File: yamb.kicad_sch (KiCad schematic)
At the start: 5 parts, among them J1 Barrel_Jack, P1 USB_C_Plug_USB2.0

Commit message: still lots of errors
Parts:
- added U1: TPS3808DBV, Package_TO_SOT_SMD:SOT-23-6, symbol Power_Supervisor:TPS3808DBV
- RAK1: value ~ -> U4
- U2: renamed from Voltaic MPPT; value ~ -> MPPT
- U3: renamed from Voltaic SVR; value ~ -> VSVR
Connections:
- net +BATT is gone; now on net BATT: U3.5 (VBAT)
- net -BATT is gone; now on net GND: U3.4 (GND)
- net +5V: now also P1.A4 (VBUS), P1.A9 (VBUS), P1.B4 (VBUS), P1.B9 (VBUS); no longer RAK1.43 (VDD_NRF), RAK1.44 (VBAT_NRF), U2.11 (VLOAD), U3.12 (VLOAD)
- net 7-20V: no longer J1.2, P1.A1 (GND), P1.A12 (GND), P1.B1 (GND), P1.B12 (GND), RAK1.14 (GND), RAK1.22 (GND), RAK1.35 (GND), RAK1.36 (GND), RAK1.42 (GND), U2.10 (GND), U2.12 (GND), U2.14 (GND), U2.16 (GND), U2.17 (GND), U3.13 (GND), U3.14 (GND), U3.16 (GND), U3.17 (GND), U3.7 (GND), U3.8 (GND)
- net SDA: now also RAK1.4 (I2C_SDA); no longer RAK1.6 (UART2_RX)
- net GND: now reaches P1.S1 (SHIELD)
- net GND: now also J1.2, P1.A1 (GND), P1.A12 (GND), P1.B1 (GND), P1.B12 (GND), RAK1.14 (GND), RAK1.16 (GND), RAK1.22 (GND), RAK1.35 (GND), RAK1.36 (GND), RAK1.38 (GND), RAK1.42 (GND), U2.10 (GND), U2.12 (GND), U2.14 (GND), U2.16 (GND), U2.17 (GND), U2.4 (GND), U2.6 (GND), U2.8 (GND), U3.13 (GND), U3.14 (GND), U3.16 (GND), U3.17 (GND), U3.7 (GND), U3.8 (GND), U1.2 (GND)
- net RESET: now reaches RAK1.17 (NRF_RESET)
- net RESET: now also U1.1 (~{RESET})
- net +3.3V: now reaches RAK1.20 (VBAT_SX)
- net +3.3V: now also RAK1.21 (VBAT_IO_SX), RAK1.43 (VDD_NRF), U2.11 (VLOAD), U2.9 (VLOAD), U3.12 (VLOAD), U1.5 (SENSE)
- net BATT: now reaches U2.5 (VBAT)
- net BATT: now also RAK1.44 (VBAT_NRF), U2.7 (VBAT)
- net 3V3 renamed 3V3_I2C
- new net VBUS: U1.6 (VDD)
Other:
- moved on the sheet: U2

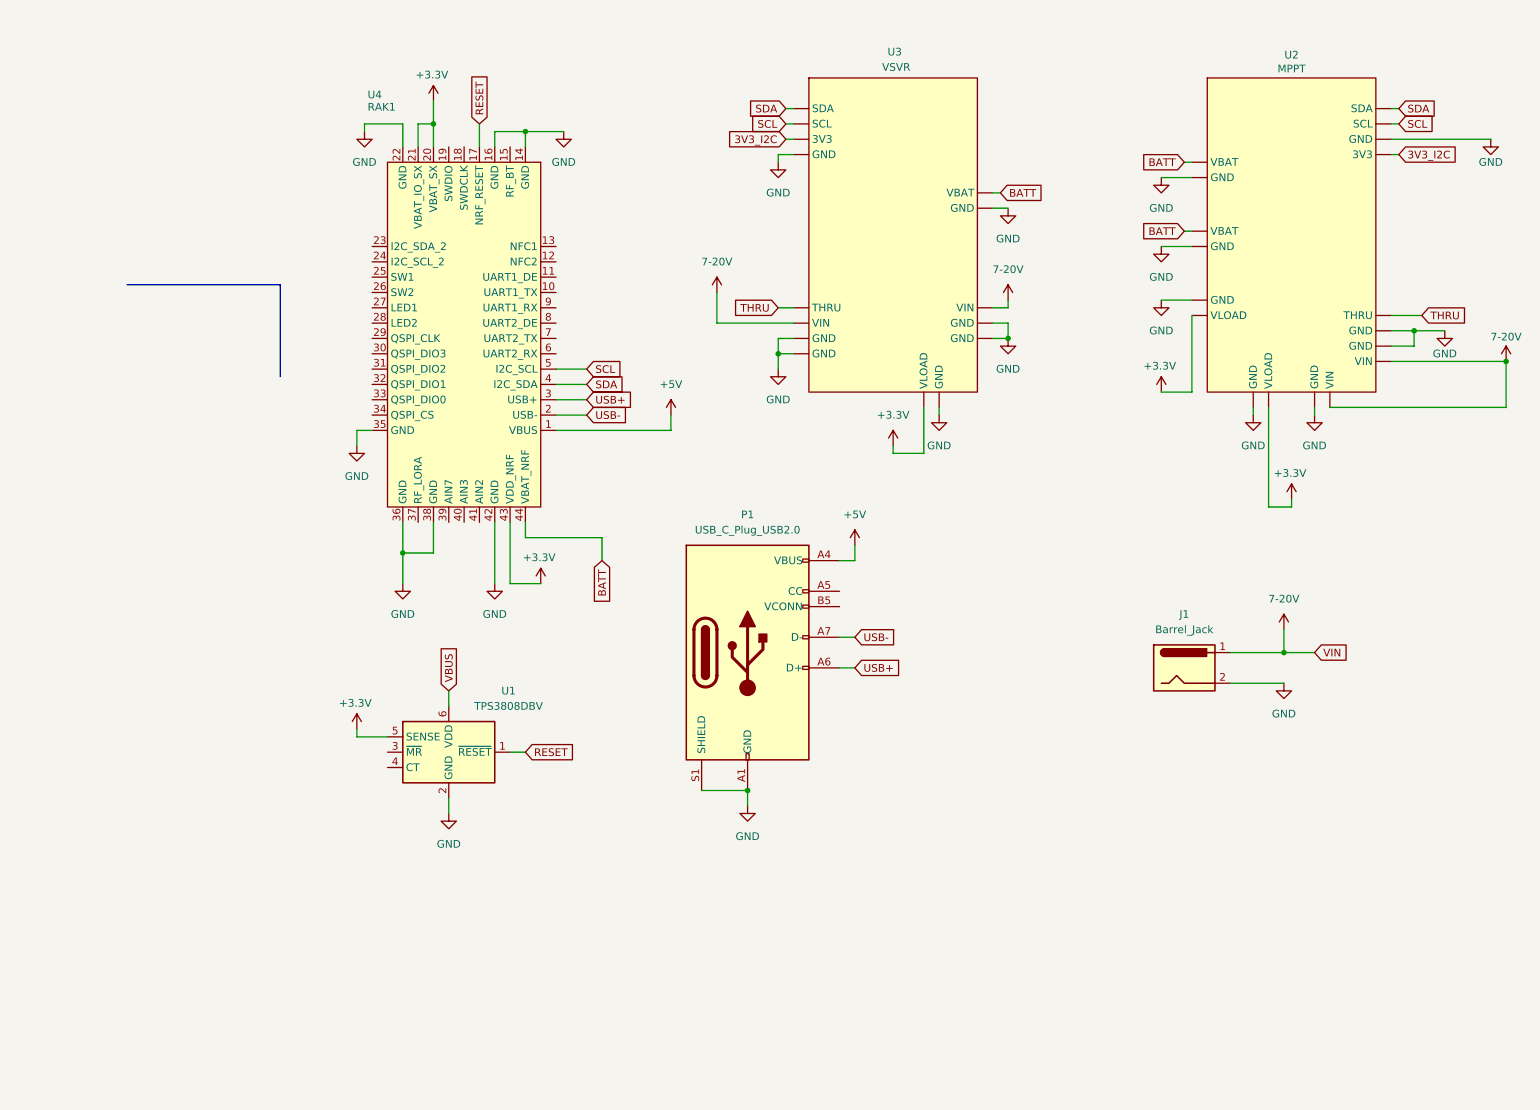
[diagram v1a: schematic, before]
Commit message: voltaic footprints, adding to schematic
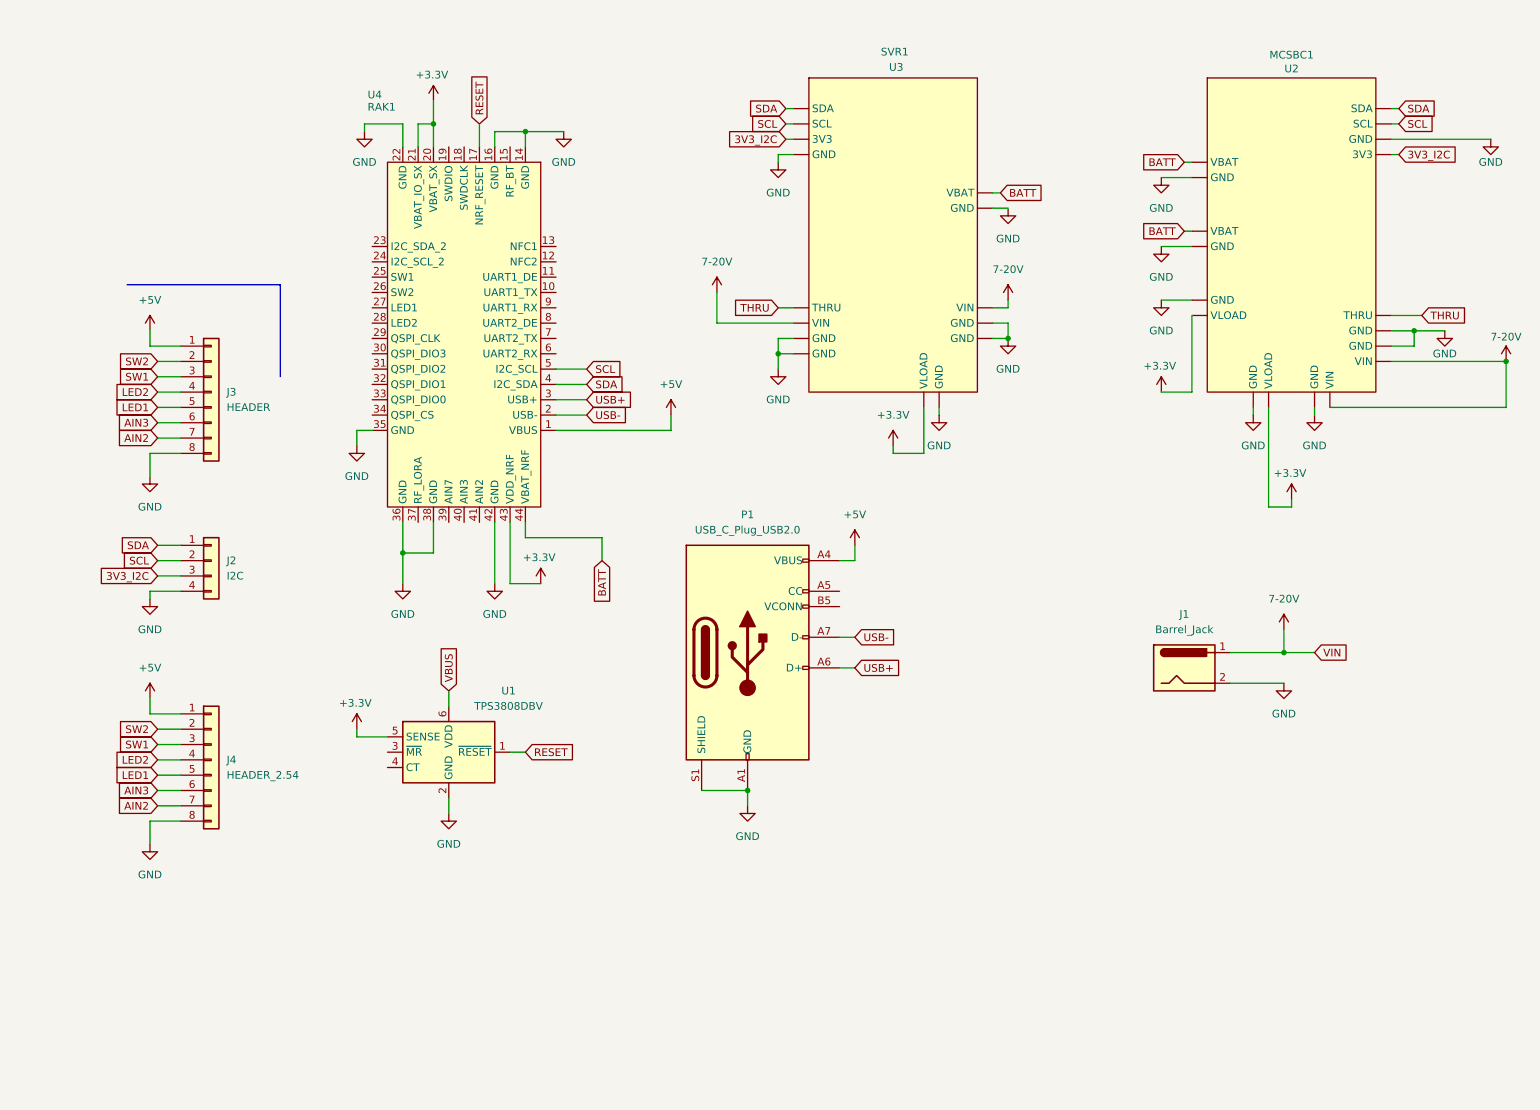
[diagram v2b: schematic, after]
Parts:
- added J2: I2C, Connector_JST:JST_PH_B4B-PH-K_1x04_P2.00mm_Vertical, symbol Connector_Generic:Conn_01x04
- added J3: HEADER, Connector_JST:JST_PH_B8B-PH-K_1x08_P2.00mm_Vertical, symbol Connector_Generic:Conn_01x08
- added J4: HEADER_2.54, Connector_PinHeader_2.54mm:PinHeader_1x08_P2.54mm_Vertical, symbol Connector_Generic:Conn_01x08
- J1: footprint (none) -> Connector_BarrelJack:SWITCHCRAFT_PC722A
- MCSBC1: renamed from U2; value MPPT -> U2; footprint (none) -> Converter_DCDC:Voltaic_MCSBC; now in the parts list
- P1: footprint (none) -> Connector_USB:USB_C_Receptacle_G-Switch_GT-USB-7051x
- RAK1: footprint (none) -> RF_Module:RAK4630
- SVR1: renamed from U3; value VSVR -> U3; footprint (none) -> Converter_DCDC:Voltaic_SVR; now in the parts list
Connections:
- net +5V: now also J3.1 (Pin_1), J4.1 (Pin_1)
- net 3V3_I2C: now also J2.3 (Pin_3)
- net GND: now also J2.4 (Pin_4), J3.8 (Pin_8), J4.8 (Pin_8)
- net SCL: now also J2.2 (Pin_2)
- net SDA: now also J2.1 (Pin_1)
- new net AIN2: J3.7 (Pin_7), J4.7 (Pin_7)
- new net AIN3: J3.6 (Pin_6), J4.6 (Pin_6)
- new net LED1: J3.5 (Pin_5), J4.5 (Pin_5)
- new net LED2: J3.4 (Pin_4), J4.4 (Pin_4)
- new net SW1: J3.3 (Pin_3), J4.3 (Pin_3)
- new net SW2: J3.2 (Pin_2), J4.2 (Pin_2)

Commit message: additional footprints for reset, power switch, correct USB-C symbol for footprint, bypass jumpers for watchdog and pwr switch
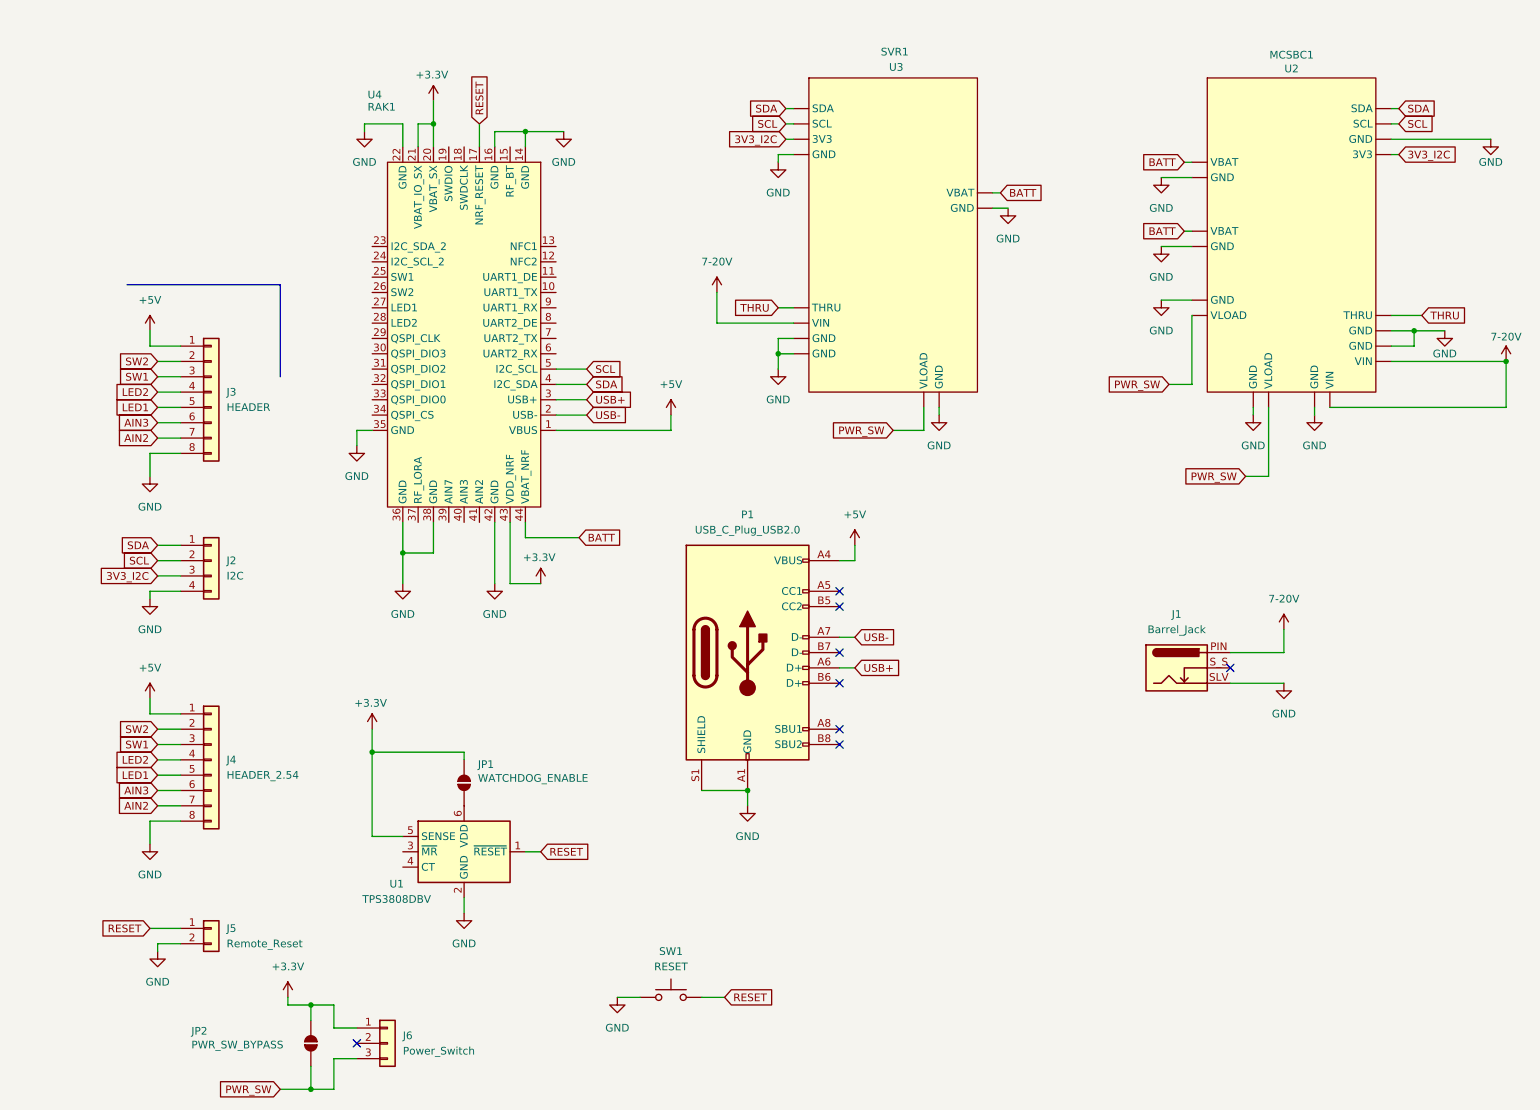
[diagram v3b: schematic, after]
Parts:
- added J5: Remote_Reset, Connector_PinHeader_1.00mm:PinHeader_1x02_P1.00mm_Vertical, symbol Connector_Generic:Conn_01x02
- added J6: Power_Switch, Connector_JST:JST_PH_B3B-PH-K_1x03_P2.00mm_Vertical, symbol Connector_Generic:Conn_01x03
- added JP1: WATCHDOG_ENABLE, Jumper:SolderJumper-2_P1.3mm_Open_RoundedPad1.0x1.5mm, symbol Jumper:SolderJumper_2_Open
- added JP2: PWR_SW_BYPASS, Jumper:SolderJumper-2_P1.3mm_Open_RoundedPad1.0x1.5mm, symbol Jumper:SolderJumper_2_Open
- added SW1: RESET, Button_Switch_THT:SW_1825910-6-4, symbol Switch:SW_Push
- J1: symbol Connector:Barrel_Jack -> Connector:Barrel_Jack_Switch
- P1: symbol Connector:USB_C_Plug_USB2.0 -> Connector:USB_C_Receptacle_USB2.0_16P
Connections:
- net +3.3V: now also J6.1 (Pin_1), JP1.1 (A), JP2.1 (A); no longer MCSBC1.11 (VLOAD), MCSBC1.9 (VLOAD), SVR1.12 (VLOAD)
- net 7-20V: now also J1.PIN, SVR1.8 (VIN); no longer J1.1, SVR1.18 (VIN), SVR1.9 (VIN)
- net GND: now also J1.SLV, SVR1.10 (GND), SVR1.11 (GND), SVR1.6 (GND), J5.2 (Pin_2), SW1.1; no longer J1.2, SVR1.13 (GND), SVR1.14 (GND), SVR1.16 (GND), SVR1.17 (GND), SVR1.8 (GND)
- net RESET: now also J5.1 (Pin_1), SW1.2
- net THRU: now also SVR1.12 (THRU); no longer SVR1.15 (THRU)
- net VBUS: no longer names the net of U1.6 (VDD)
- net VBUS: now also JP1.2 (B)
- new net PWR_SW: J6.3 (Pin_3), JP2.2 (B), MCSBC1.11 (VLOAD), MCSBC1.9 (VLOAD), SVR1.9 (VLOAD)
- no-connect marks 0 -> 8
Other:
- moved on the sheet: U1

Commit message: custom libraries
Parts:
- J3: footprint Connector_JST:JST_PH_B8B-PH-K_1x08_P2.00mm_Vertical -> Connector_JST:JST_PHD_B16B-PHDSS_2x08_P2.00mm_Vertical; symbol Connector_Generic:Conn_01x08 -> Connector_Generic:Conn_02x08_Odd_Even
- J4: footprint Connector_PinHeader_2.54mm:PinHeader_1x08_P2.54mm_Vertical -> Connector_PinHeader_2.54mm:PinHeader_2x08_P2.54mm_Vertical; symbol Connector_Generic:Conn_01x08 -> Connector_Generic:Conn_02x08_Odd_Even
- SW1: symbol Switch:SW_Push -> Switch:SW_Push_Dual
- U2: renamed from MCSBC1; value U2 -> MCSBC; symbol Regulator_Controller:VOLTAIC_SOLAR_1 -> Andy_Symbols:VOLTAIC_MCSBC
- U3: renamed from SVR1; value U3 -> SVR; footprint Converter_DCDC:Voltaic_SVR -> Andy_Footprints:Voltaic_SVR; symbol Regulator_Controller:VOLTAIC_SVR -> Andy_Symbols:VOLTAIC_SVR
- U4: renamed from RAK1; value U4 -> RAK4630; footprint RF_Module:RAK4630 -> Andy_Footprints:RAK4630; symbol RF_Module:RAK4630 -> Andy_Symbols:RAK4630
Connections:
- net +3.3V: now also J3.1 (Pin_1), J4.1 (Pin_1), U3.9 (VOUT)
- net 7-20V: now also J1.1, U2.5 (SVC_VOUT); no longer J1.PIN, U2.13 (VIN), U2.18 (VIN)
- net AIN2: now also J3.13 (Pin_13), J4.13 (Pin_13), U4.41 (AIN2); no longer J3.7 (Pin_7), J4.7 (Pin_7)
- net AIN3: now also J3.11 (Pin_11), J4.11 (Pin_11), U4.40 (AIN3); no longer J3.6 (Pin_6), J4.6 (Pin_6)
- net GND: now also J1.2, J3.15 (Pin_15), J4.15 (Pin_15), U2.2 (GND), U2.7 (GND); no longer J1.SLV, J3.8 (Pin_8), J4.8 (Pin_8), U2.10 (GND), U2.12 (GND), U2.14 (GND), U2.16 (GND), U2.17 (GND), U2.4 (GND), U2.8 (GND)
- net LED1: now also J3.9 (Pin_9), J4.9 (Pin_9), U4.27 (LED1); no longer J3.5 (Pin_5), J4.5 (Pin_5)
- net LED2: now also J3.7 (Pin_7), J4.7 (Pin_7), U4.28 (LED2); no longer J3.4 (Pin_4), J4.4 (Pin_4)
- net SCL: no longer U2.2 (SCL)
- net SDA: no longer U2.1 (SDA)
- net SW1: now also J3.5 (Pin_5), J4.5 (Pin_5), U4.25 (SW1); no longer J3.3 (Pin_3), J4.3 (Pin_3)
- net SW2: now also J3.3 (Pin_3), J4.3 (Pin_3), U4.26 (SW2); no longer J3.2 (Pin_2), J4.2 (Pin_2)
- net THRU: now also U2.8 (SVC_VIN); no longer U2.15 (THRU)
- net UART_TX: now reaches U4.10 (UART1_TX)
- net UART_TX: now also J3.2 (Pin_2), J4.2 (Pin_2)
- net UAART_RX: now reaches U4.9 (UART1_RX)
- net UAART_RX: now also J3.4 (Pin_4), J4.4 (Pin_4)
- net +5V renamed VBUS
- net VBUS: no longer J3.1 (Pin_1), J4.1 (Pin_1)
- net 3V3_I2C renamed 3V3
- net 3V3: now also J6.3 (Pin_3), JP2.2 (B); no longer U2.3 (3V3)
- net BATT renamed +BATT
- net +BATT: now also U2.1 (VBAT); no longer U2.5 (VBAT), U2.7 (VBAT)
- removed net PWR_SW: J6.3 (Pin_3), JP2.2 (B), U2.11 (VLOAD), U2.9 (VLOAD), U3.9 (VLOAD)
- no-connect marks 8 -> 45
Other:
- moved on the sheet: J1, J2, J5, J6, JP1, JP2, P1, U1, U4
